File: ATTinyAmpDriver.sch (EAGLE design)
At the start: 22 parts, among them Q1 SI2301CDS, T1 BC846, U1 SPX5205M5-L-3-3, U2 ATTINY5-TSHR, U3 MCP6001, X1 DIODES, X2 INPUT

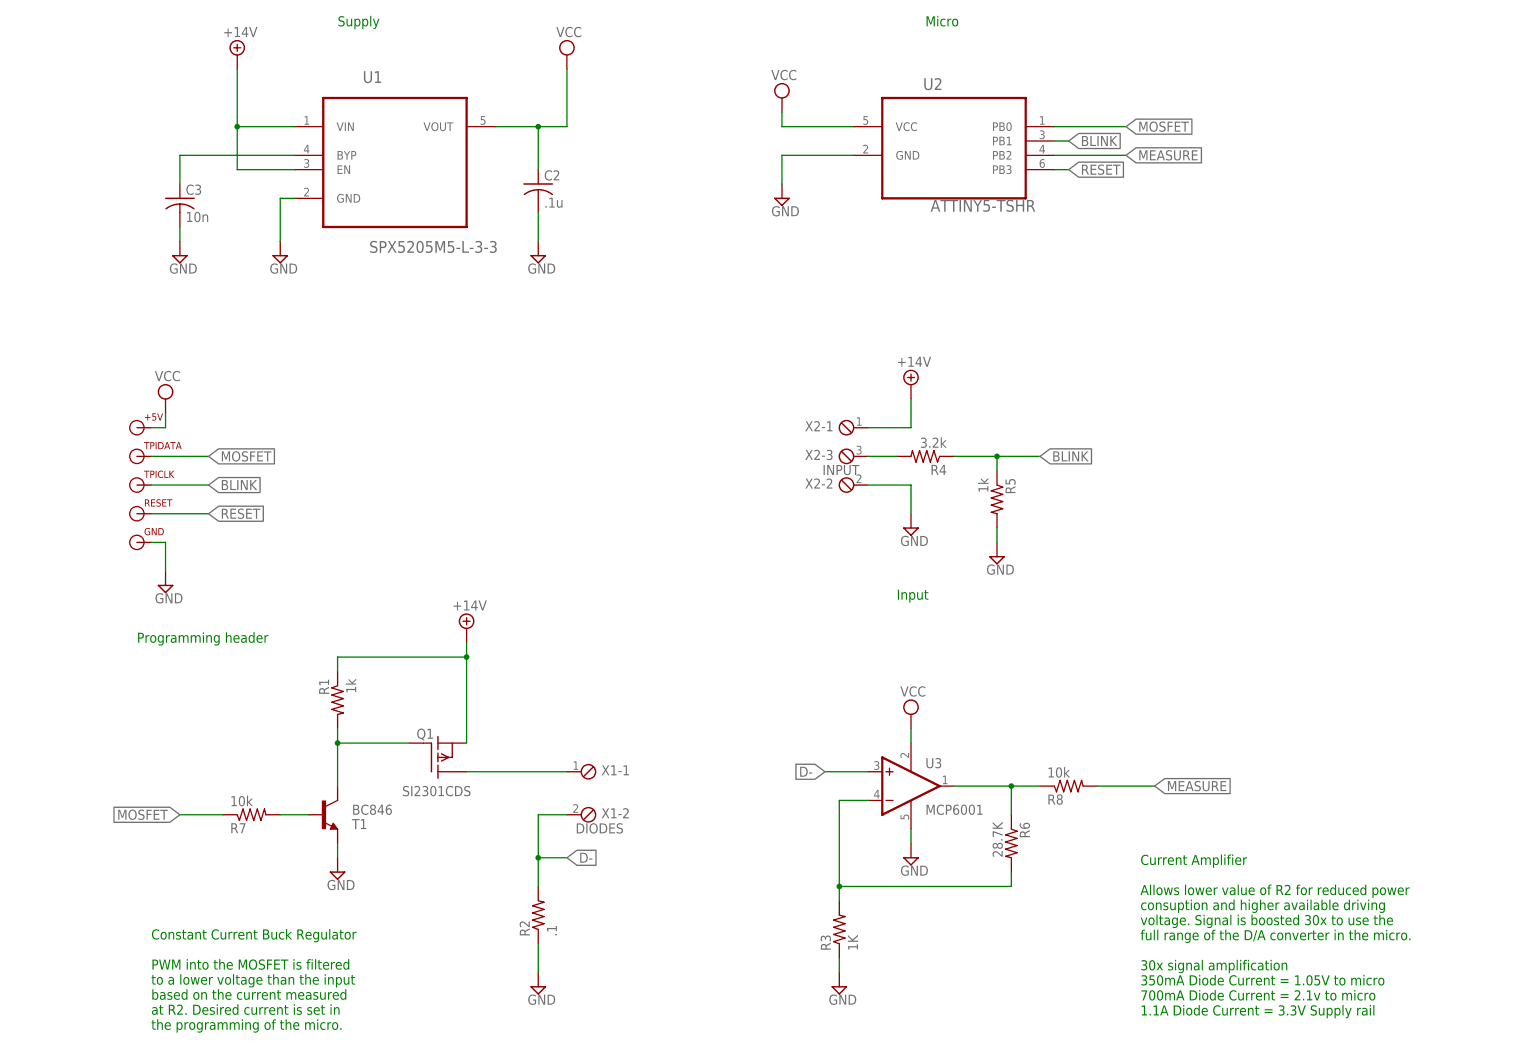
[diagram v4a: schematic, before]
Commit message: Low Pass filter before OpAmp
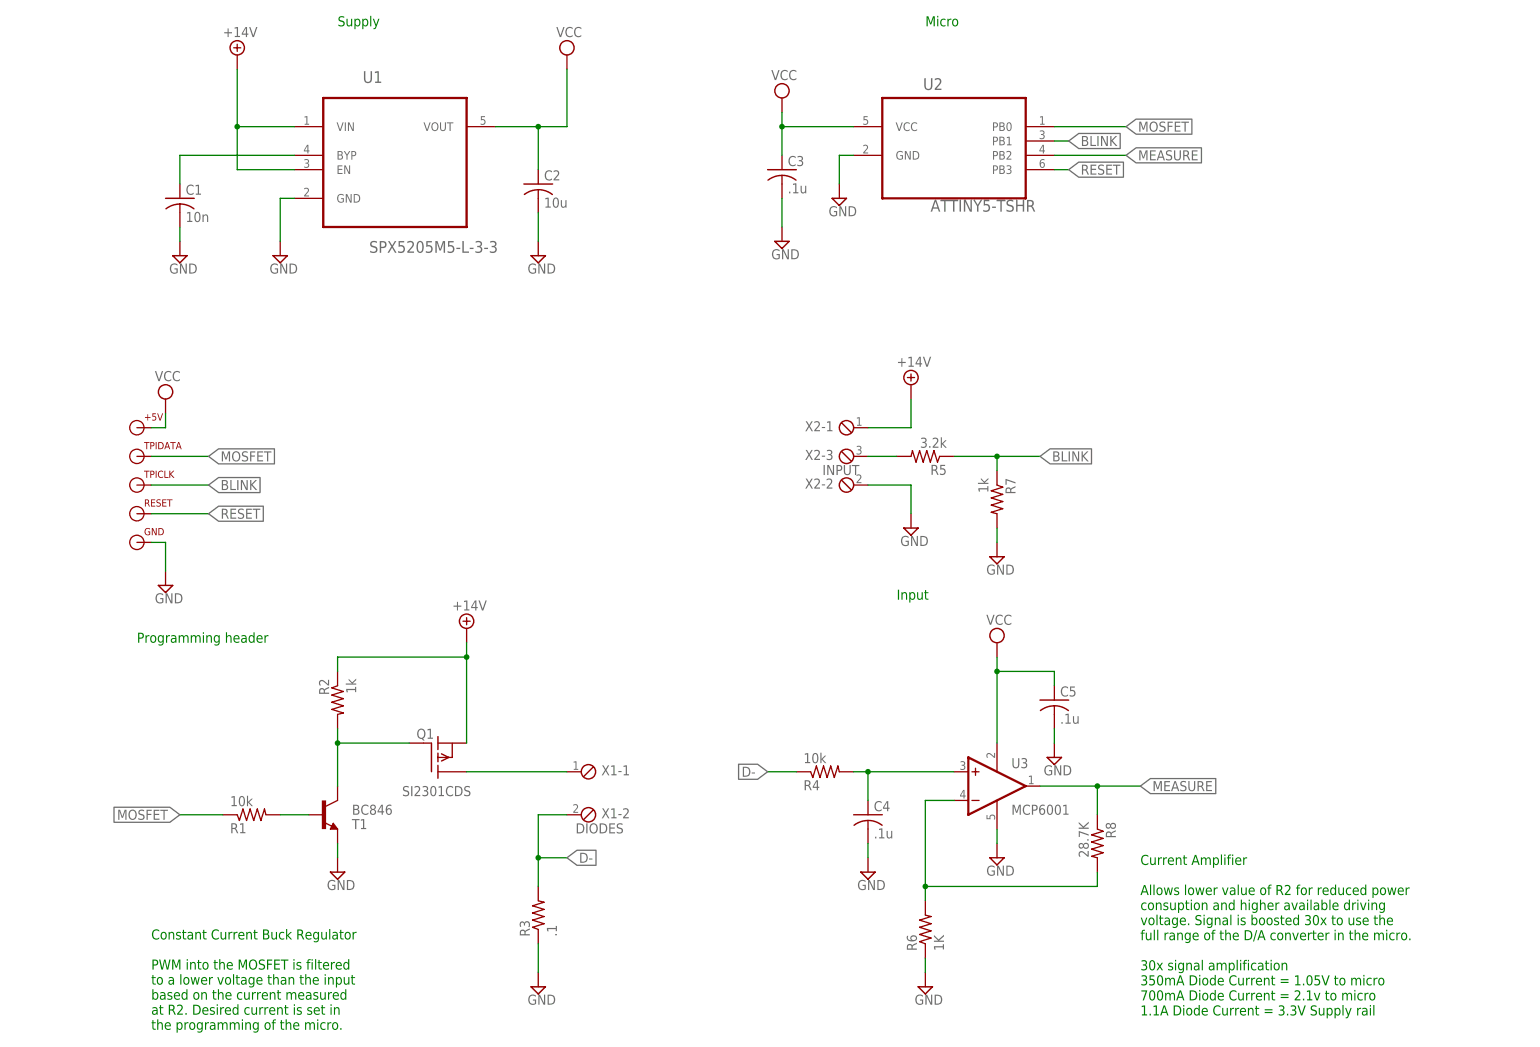
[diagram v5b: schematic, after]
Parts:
- added C1: 10n, resistor:C-USC0603
- added C4, C5: .1u, resistor:C-USC0603
- C2: value .1u -> 10u
- C3: value 10n -> .1u; DIGIKEY 445-1311-1-ND -> 445-1316-1-ND
- R1: value 1k -> 10k; device resistor:R-US_R1206 -> resistor:R-US_R0603
- R2: value .1 -> 1k; device resistor:R-US_R1206 -> resistor:R-US_R0603; DIGIKEY A103268CT-ND -> RMCF1206JT10K0CT-ND; DIGIKEY_COST .13 -> .05
- R3: value 1K -> .1; device resistor:R-US_R0603 -> resistor:R-US_R1206; DIGIKEY RMCF0603JT1K00CT-ND -> A103268CT-ND; DIGIKEY_COST .02 -> .13
- R4: value 3.2k -> 10k; device resistor:R-US_R1206 -> resistor:R-US_R0603; DIGIKEY RMCF1206JT910RCT-ND -> RMCF1206JT10K0CT-ND
- R5: value 1k -> 3.2k; device resistor:R-US_R1206 -> resistor:R-US_R0603; DIGIKEY RMCF1206JT300RCT-ND -> RMCF1206JT910RCT-ND
- R6: value 28.7K -> 1K; DIGIKEY RMCF0603FT28R7CT-ND -> RMCF0603JT1K00CT-ND; DIGIKEY_COST .04 -> .02
- R7: value 10k -> 1k; device resistor:R-US_R1206 -> resistor:R-US_R0603; DIGIKEY RMCF1206JT10K0CT-ND -> RMCF1206JT300RCT-ND
- R8: value 10k -> 28.7K; device resistor:R-US_R1206 -> resistor:R-US_R0603; DIGIKEY RMCF1206JT10K0CT-ND -> RMCF0603FT28R7CT-ND; DIGIKEY_COST .05 -> .04
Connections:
- removed net OPAMP_OUT: R6.1, R8.1, U3.OUT
- new net N$7: C4.1, R4.2, U3.+IN
- net +14V: now also R2.1; no longer R1.1
- net BLINK: now also R7.1; no longer R4.1
- net D-: now also R3.2, R4.1; no longer R2.2, U3.+IN
- net GND: now also C1.2, C4.2, C5.2, R6.1, R7.2; no longer R2.1, R5.2
- net MEASURE: now also R8.1, U3.OUT; no longer R8.2
- net MOSFET: now also R1.1; no longer R7.1
- net N$1: now also R5.2; no longer R4.2
- net N$2: now also C1.1; no longer C3.1
- net N$4: now also R8.2; no longer R3.2
- net N$5: now also R2.2; no longer R1.2
- net N$6: now also R1.2; no longer R7.2
- net VCC: now also C3.1, C5.1
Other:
- moved on the sheet: C3, R1, R2, R3, R4, R5, R6, R7, R8, U3

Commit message: Changed PWM filter to Sallen Key
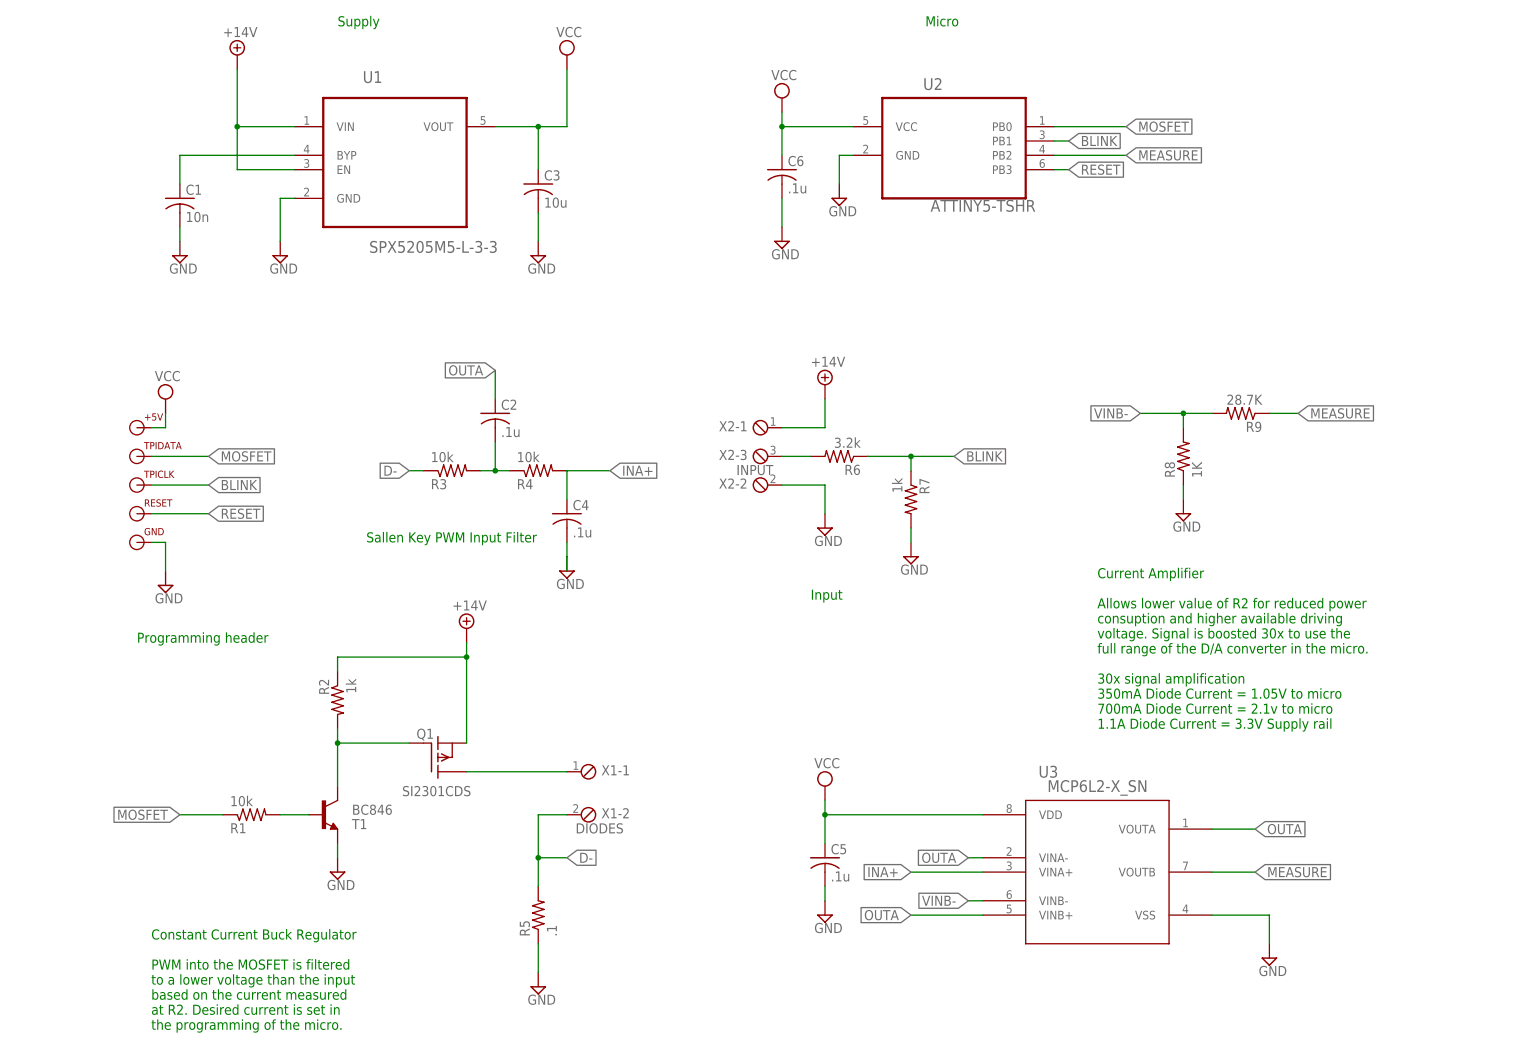
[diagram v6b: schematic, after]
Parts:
- added C6: .1u, resistor:C-USC0603
- added R9: 28.7K, resistor:R-US_R0603
- C2: value 10u -> .1u; device resistor:C-USC0805 -> resistor:C-USC0603; DIGIKEY 445-7534-1-ND -> 445-1316-1-ND
- C3: value .1u -> 10u; device resistor:C-USC0603 -> resistor:C-USC0805; DIGIKEY 445-1316-1-ND -> 445-7534-1-ND
- R3: value .1 -> 10k; device resistor:R-US_R1206 -> resistor:R-US_R0603; DIGIKEY A103268CT-ND -> RMCF1206JT10K0CT-ND; DIGIKEY_COST .13 -> .05
- R5: value 3.2k -> .1; device resistor:R-US_R0603 -> resistor:R-US_R1206; DIGIKEY RMCF1206JT910RCT-ND -> A103268CT-ND; DIGIKEY_COST .05 -> .13
- R6: value 1K -> 3.2k; DIGIKEY RMCF0603JT1K00CT-ND -> RMCF1206JT910RCT-ND; DIGIKEY_COST .02 -> .05
- R8: value 28.7K -> 1K; DIGIKEY RMCF0603FT28R7CT-ND -> RMCF0603JT1K00CT-ND; DIGIKEY_COST .04 -> .02
- U3: value MCP6001 -> MCP6L2-X_SN; device Combined:MCP6001 -> Combined:MCP6L2-X_SN; DIGIKEY MCP6001T-I/OTCT-ND -> MCP6L2T-E/SNCT-ND; DIGIKEY_COST .29 -> .64
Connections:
- removed net N$4: R6.2, R8.2, U3.-IN
- removed net N$7: C4.1, R4.2, U3.+IN
- new net INA+: C4.1, R4.2, U3.VINA+
- new net N$8: C2.2, R3.2, R4.1
- new net OUTA: C2.1, U3.VINA-, U3.VINB+, U3.VOUTA
- new net VINB-: R8.2, R9.2, U3.VINB-
- net BLINK: now also R6.1; no longer R5.1
- net D-: now also R3.1, R5.2; no longer R3.2, R4.1
- net GND: now also C6.2, R5.1, R8.1, U3.VSS; no longer C2.2, R3.1, R6.1, U3.V-
- net MEASURE: now also R9.1, U3.VOUTB; no longer R8.1, U3.OUT
- net N$1: now also R6.2; no longer R5.2
- net VCC: now also C6.1, U3.VDD; no longer C2.1, U3.V+
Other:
- note added: "Sallen Key PWM Input Filter"
- moved on the sheet: C2, C3, C4, C5, R3, R4, R5, R6, R7, R8, X2-1, X2-2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

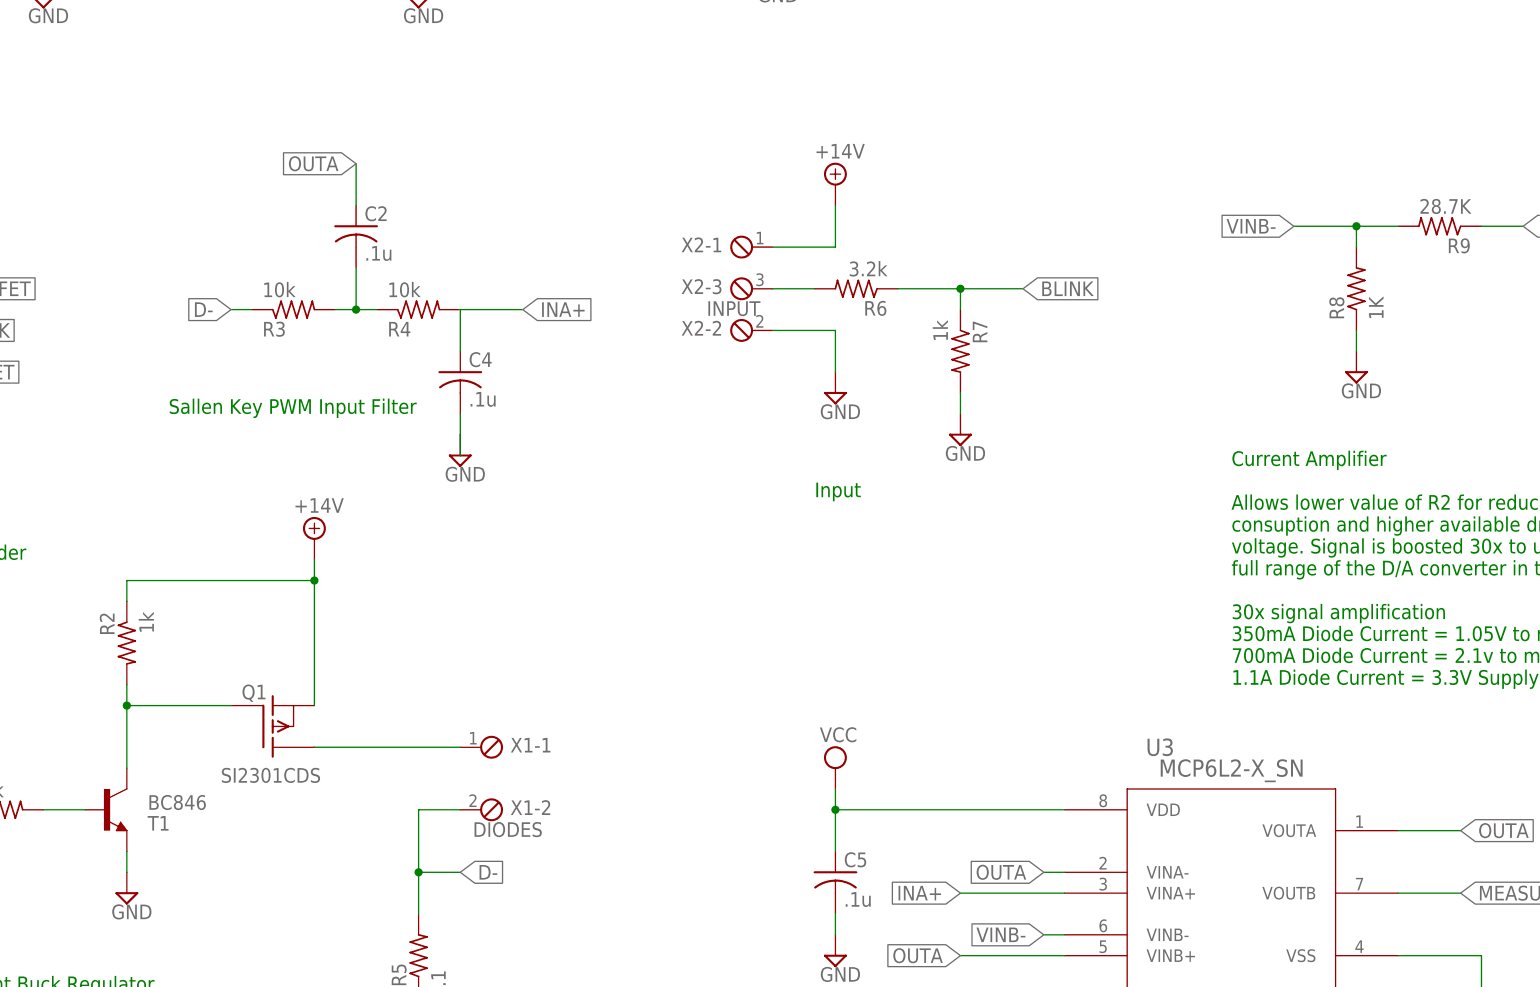
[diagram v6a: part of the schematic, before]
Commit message: Added a diode to Blink input to prevent back feed if transistor shorts
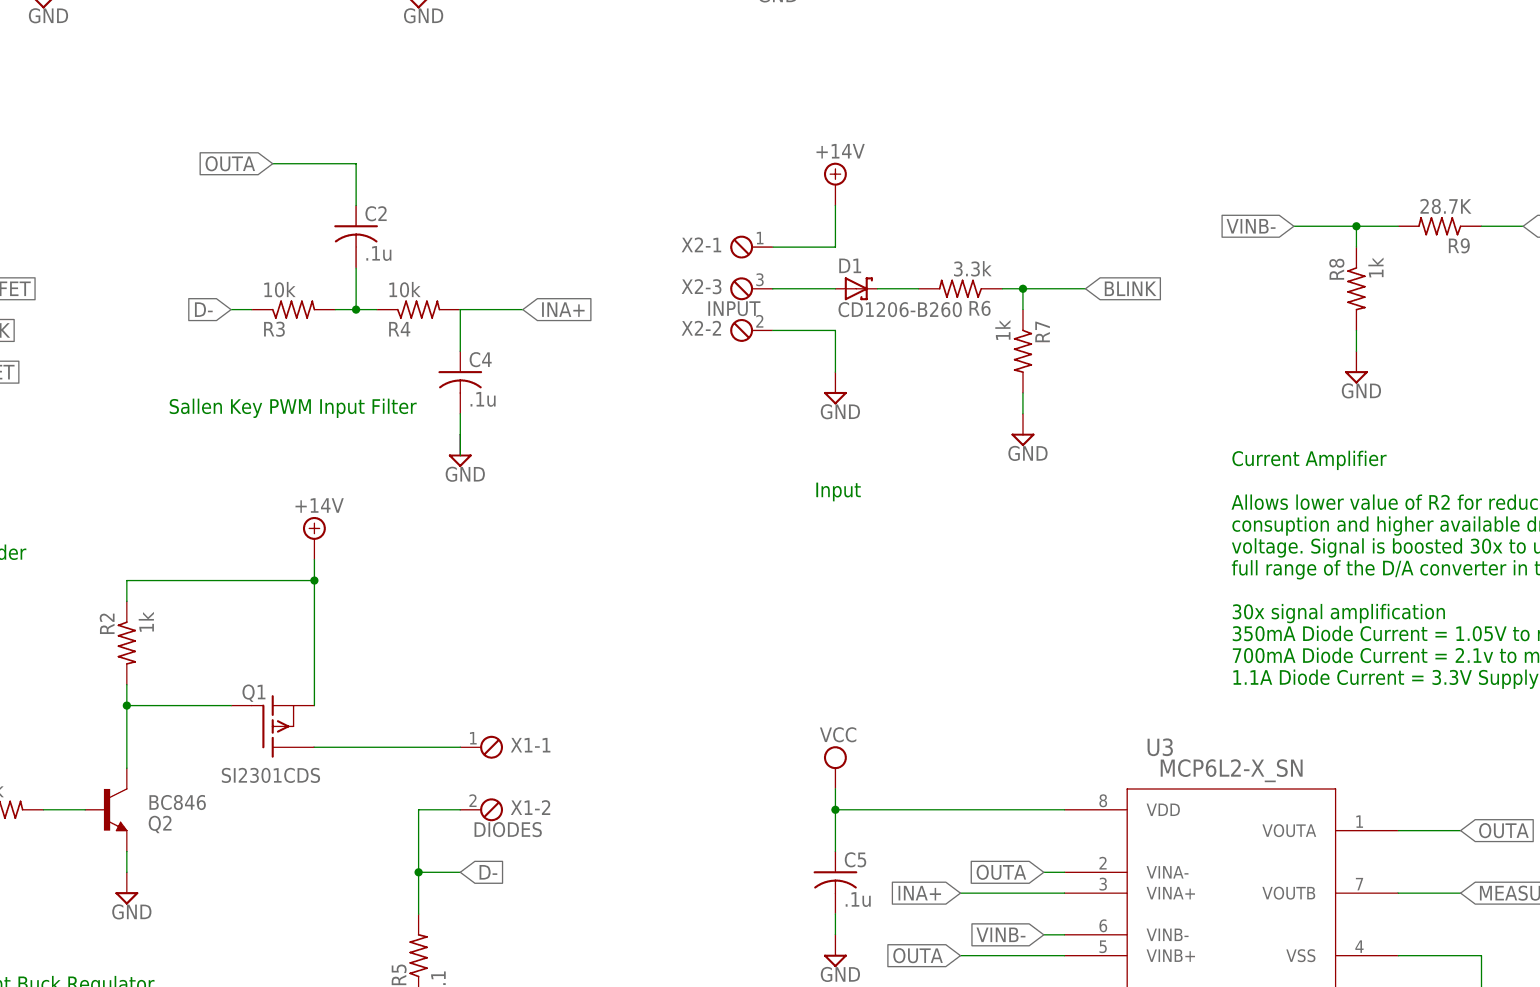
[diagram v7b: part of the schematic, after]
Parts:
- added D1: CD1206-B260, Combined:CD1206-B260
- Q2: DIGIKEY (none) -> BC846BMTFCT-ND; DIGIKEY_COST (none) -> .17
- R1, R3, R4: DIGIKEY RMCF1206JT10K0CT-ND -> RMCF0603FT10K0CT-ND; DIGIKEY_COST .05 -> .04
- R2: DIGIKEY RMCF1206JT10K0CT-ND -> RMCF0603FT1K00CT-ND; DIGIKEY_COST .05 -> .04
- R6: value 3.2k -> 3.3k; DIGIKEY RMCF1206JT910RCT-ND -> RMCF0603FT3K30CT-ND; DIGIKEY_COST .05 -> .04
- R7: DIGIKEY RMCF1206JT300RCT-ND -> RMCF0603FT1K00CT-ND; DIGIKEY_COST .05 -> .04
- R8: value 1K -> 1k; DIGIKEY RMCF0603JT1K00CT-ND -> RMCF0603FT1K00CT-ND; DIGIKEY_COST .02 -> .04
- renumbered T1 to Q2
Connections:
- new net N$4: D1.C, R6.2
- net GND: now also R8.2; no longer R8.1
- net N$1: now also D1.A; no longer R6.2
- net VINB-: now also R8.1; no longer R8.2
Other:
- moved on the sheet: R6, R7, R8
